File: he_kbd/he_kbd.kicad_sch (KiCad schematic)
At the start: 54 parts, among them J1 AudioJack4, J2 Conn_01x08_Pin

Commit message: updating schematic, realised missing changes from other branch
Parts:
- removed R7, R8, R9: 10k, Resistor_SMD:R_0805_2012Metric_Pad1.20x1.40mm_HandSolder, symbol PCM_SL_Resistors:10k
- added C10, C11, C12, C13, C14, C15, C16, C17, C18, C19, C20, C21, C22, C23, C24, C25, C26, C27, C28, C29, C3, C30, C31, C32, C33, C34, C35, C36, C37, C4, C5, C6, C7, C8, C9: 100n, PCM_Capacitor_SMD_AKL:C_0805_2012Metric_Pad1.18x1.45mm_HandSolder, symbol PCM_Capacitor_AKL:C_0805
- added C38: 500u, PCM_Capacitor_SMD_AKL:C_0805_2012Metric_Pad1.18x1.45mm_HandSolder, symbol PCM_Capacitor_US_AKL:C_0805
- added C39: 100u, PCM_Capacitor_SMD_AKL:C_0805_2012Metric_Pad1.18x1.45mm_HandSolder, symbol PCM_Capacitor_US_AKL:C_0805
- added C40: 50u, PCM_Capacitor_SMD_AKL:C_0805_2012Metric_Pad1.18x1.45mm_HandSolder, symbol PCM_Capacitor_US_AKL:C_0805
- added C41: 20u, PCM_Capacitor_SMD_AKL:C_0805_2012Metric_Pad1.18x1.45mm_HandSolder, symbol PCM_Capacitor_US_AKL:C_0805
- added C42: 10u, PCM_Capacitor_SMD_AKL:C_0805_2012Metric_Pad1.18x1.45mm_HandSolder, symbol PCM_Capacitor_US_AKL:C_0805
- added C51, C_MTP1, C_MTP2, C_MTP3: 100n, PCM_Capacitor_SMD_AKL:C_0805_2012Metric_Pad1.18x1.45mm_HandSolder, symbol PCM_Capacitor_US_AKL:C_0805
- added D1, D10, D11, D12, D13, D14, D15, D16, D17, D18, D19, D2, D20, D21, D22, D23, D24, D25, D26, D27, D28, D29, D3, D30, D31, D32, D33, D34, D35, D4, D5, D6, D7, D8, D9: WS2812B, LED_SMD:LED_WS2812B_PLCC4_5.0x5.0mm_P3.2mm, symbol LED:WS2812B
- added R1, R10, R14, R2, R3: 420, Resistor_SMD:R_0805_2012Metric_Pad1.20x1.40mm_HandSolder, symbol PCM_SL_Resistors:10k
- added SW1, SW10, SW11, SW12, SW13, SW14, SW15, SW16, SW17, SW18, SW19, SW2, SW20, SW21, SW22, SW23, SW24, SW25, SW26, SW27, SW28, SW29, SW3, SW30, SW31, SW32, SW33, SW34, SW35, SW4, SW5, SW6, SW7, SW8, SW9: ~, he_kbd_footprint:SW_Cherry_MX_1.00u_ANALOGUE, symbol he_lib:1u_switch_profile
- C43: value 50u -> 500u
- C44: value 50u -> 100u
- C45, C50: value 50u -> 1u
- C47: value 50u -> 20u
- C48: value 50u -> 100n
- C49: value 50u -> 10u
- R5, R6: value 4.7k -> 10k
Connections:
- net MTP_EN_0 is gone; now on net ANALOGUE_GND: A1.6 (GPIO4), AM0.15 (~{E})
- net MTP_EN_1 is gone; now on net ANALOGUE_GND: A1.7 (GPIO5), AM1.15 (~{E})
- net MTP_EN_2 is gone; now on net ANALOGUE_GND: A1.9 (GPIO6), AM2.15 (~{E})
- net MTP_BIN_0: now also R1.1; no longer A1.1 (GPIO0)
- net MTP_BIN_1: now also R2.1; no longer A1.2 (GPIO1)
- net MTP_BIN_2: now also R3.1; no longer A1.4 (GPIO2)
- net MTP_BIN_3: now also R10.1; no longer A1.5 (GPIO3)
- net NEOPIXEL_DATA: now also R14.1
- net ADC_1: now reaches A1.32 (GPIO27_ADC1)
- net ADC_1: now also AM1.1 (COM)
- net ADC_2: now reaches A1.34 (GPIO28_ADC2)
- net ADC_2: now also AM2.1 (COM)
- net LOCAL_VIN: now reaches A1.40 (VBUS)
- net LOCAL_VIN: now also C45.2, C10.1, C11.1, C12.1, C13.1, C14.1, C15.1, C16.1, C17.1, C18.1, C19.1, C20.1, C21.1, C22.1, C23.1, C24.1, C25.1, C26.1, C27.1, C28.1, C29.1, C3.1, C30.1, C31.1, C32.1, C33.1, C34.1, C35.1, C36.1, C37.1, C38.2, C39.2, C4.1, C40.2, C41.2, C42.2, C5.1, C51.2, C6.1, C7.1, C8.1, C9.1, D1.1 (VDD), D10.1 (VDD), D11.1 (VDD), D12.1 (VDD), D13.1 (VDD), D14.1 (VDD), D15.1 (VDD), D16.1 (VDD), D17.1 (VDD), D18.1 (VDD), D19.1 (VDD), D2.1 (VDD), D20.1 (VDD), D21.1 (VDD), D22.1 (VDD), D23.1 (VDD), D24.1 (VDD), D25.1 (VDD), D26.1 (VDD), D27.1 (VDD), D28.1 (VDD), D29.1 (VDD), D3.1 (VDD), D30.1 (VDD), D31.1 (VDD), D32.1 (VDD), D33.1 (VDD), D34.1 (VDD), D35.1 (VDD), D4.1 (VDD), D5.1 (VDD), D6.1 (VDD), D7.1 (VDD), D8.1 (VDD), D9.1 (VDD)
- net ANALOGUE_VIN renamed 3V3
- net 3V3: now also J1.T, R5.2, R6.1, C_MTP1.2, C_MTP2.2; no longer C45.1
- net AN_SIG renamed ADC_0
- net ADC_0: no longer AM1.1 (COM), AM2.1 (COM)
- net GND renamed ANALOGUE_GND
- net ANALOGUE_GND: now also C45.1, C38.1, C39.1, C40.1, C41.1, C42.1, C51.1, C_MTP1.1, C_MTP2.1, C_MTP3.1; no longer C45.2
- net I2C0_SCL renamed I2C_0_SCL
- net I2C0_SDA renamed I2C_0_SDA
- removed net NEOPIXEL_POWER: A1.39 (VSYS), J1.T, R5.2, R6.1
- new net: D12.2 (DOUT), D13.4 (DIN)
- new net: D11.2 (DOUT), D12.4 (DIN)
- new net: D16.2 (DOUT), D17.4 (DIN)
- new net: D15.2 (DOUT), D16.4 (DIN)
- new net: D8.2 (DOUT), D9.4 (DIN)
- new net: D7.2 (DOUT), D8.4 (DIN)
- new net: A1.1 (GPIO0), R1.2
- new net: A1.5 (GPIO3), R10.2
- new net: D22.2 (DOUT), D23.4 (DIN)
- new net: D21.2 (DOUT), D22.4 (DIN)
- new net: D13.2 (DOUT), D14.4 (DIN)
- new net: D18.2 (DOUT), D19.4 (DIN)
- new net: D17.2 (DOUT), D18.4 (DIN)
- new net: D1.2 (DOUT), D2.4 (DIN)
- new net: D1.4 (DIN), R14.2
- new net: D6.2 (DOUT), D7.4 (DIN)
- new net: D5.2 (DOUT), D6.4 (DIN)
- new net: D4.2 (DOUT), D5.4 (DIN)
- new net: D25.2 (DOUT), D26.4 (DIN)
- new net: D24.2 (DOUT), D25.4 (DIN)
- new net: D27.2 (DOUT), D28.4 (DIN)
- new net: D26.2 (DOUT), D27.4 (DIN)
- new net: D3.2 (DOUT), D4.4 (DIN)
- new net: A1.2 (GPIO1), R2.2
- new net: A1.4 (GPIO2), R3.2
- new net: D14.2 (DOUT), D15.4 (DIN)
- new net: D34.2 (DOUT), D35.4 (DIN)
- new net: D33.2 (DOUT), D34.4 (DIN)
- new net: D19.2 (DOUT), D20.4 (DIN)
- new net: D10.4 (DIN), D9.2 (DOUT)
- new net: D23.2 (DOUT), D24.4 (DIN)
- new net: D32.2 (DOUT), D33.4 (DIN)
- new net: D10.2 (DOUT), D11.4 (DIN)
- new net: D30.2 (DOUT), D31.4 (DIN)
- new net: D29.2 (DOUT), D30.4 (DIN)
- new net: D28.2 (DOUT), D29.4 (DIN)
- new net: D31.2 (DOUT), D32.4 (DIN)
- new net: D20.2 (DOUT), D21.4 (DIN)
- new net: D2.2 (DOUT), D3.4 (DIN)
- new net LOCAL_GND: C10.2, C11.2, C12.2, C13.2, C14.2, C15.2, C16.2, C17.2, C18.2, C19.2, C20.2, C21.2, C22.2, C23.2, C24.2, C25.2, C26.2, C27.2, C28.2, C29.2, C3.2, C30.2, C31.2, C32.2, C33.2, C34.2, C35.2, C36.2, C37.2, C4.2, C5.2, C6.2, C7.2, C8.2, C9.2, D1.3 (VSS), D10.3 (VSS), D11.3 (VSS), D12.3 (VSS), D13.3 (VSS), D14.3 (VSS), D15.3 (VSS), D16.3 (VSS), D17.3 (VSS), D18.3 (VSS), D19.3 (VSS), D2.3 (VSS), D20.3 (VSS), D21.3 (VSS), D22.3 (VSS), D23.3 (VSS), D24.3 (VSS), D25.3 (VSS), D26.3 (VSS), D27.3 (VSS), D28.3 (VSS), D29.3 (VSS), D3.3 (VSS), D30.3 (VSS), D31.3 (VSS), D32.3 (VSS), D33.3 (VSS), D34.3 (VSS), D35.3 (VSS), D4.3 (VSS), D5.3 (VSS), D6.3 (VSS), D7.3 (VSS), D8.3 (VSS), D9.3 (VSS)
- new net VSYS: A1.39 (VSYS)
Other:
- removed sheet Switch profiles
- removed sheet leds
- note added: "Hall effect Sensors - GH39FKSW"
- note added: "Neopixels"
- note added: "Raspberry Pi Pico - rp2040"
- note removed: "Hall effect Sensors / Transistors"
- moved on the sheet: A1, AM0, AM1, AM2, C43, C44, C46, C47, C48, C49, C50, HE_1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

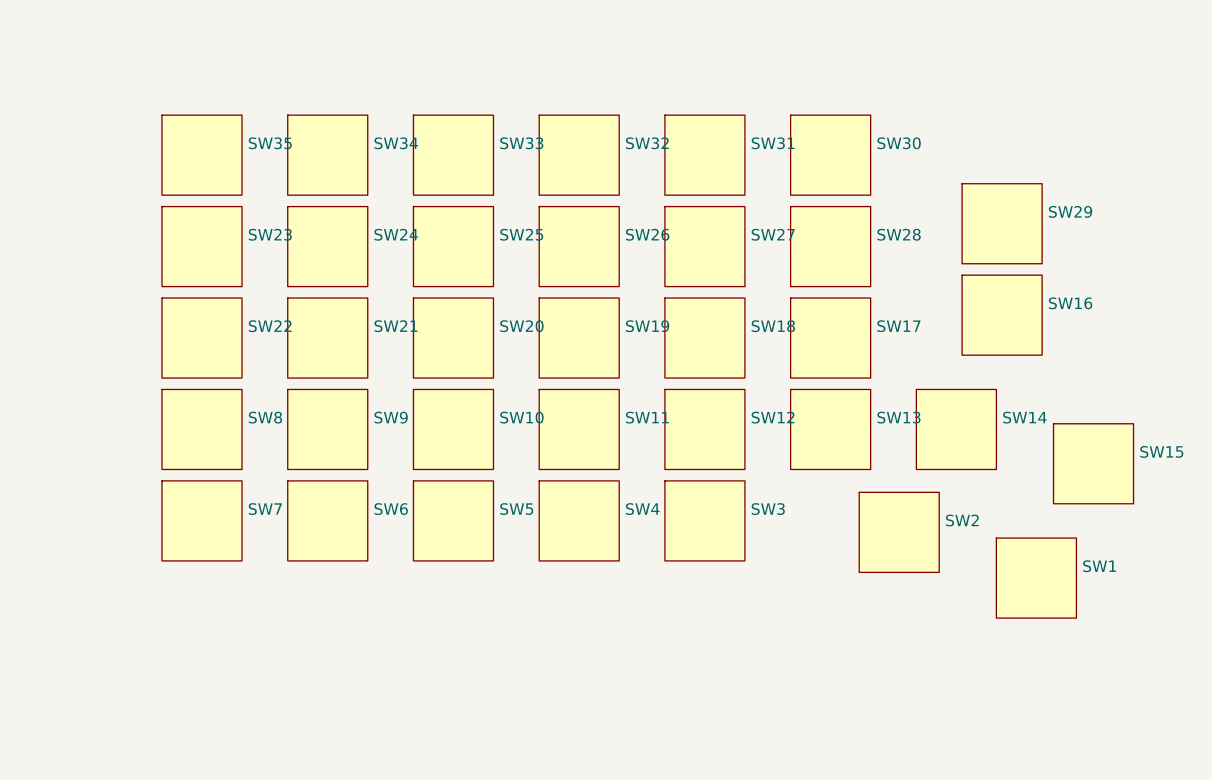
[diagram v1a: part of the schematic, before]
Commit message: tested footprint, updated schematics
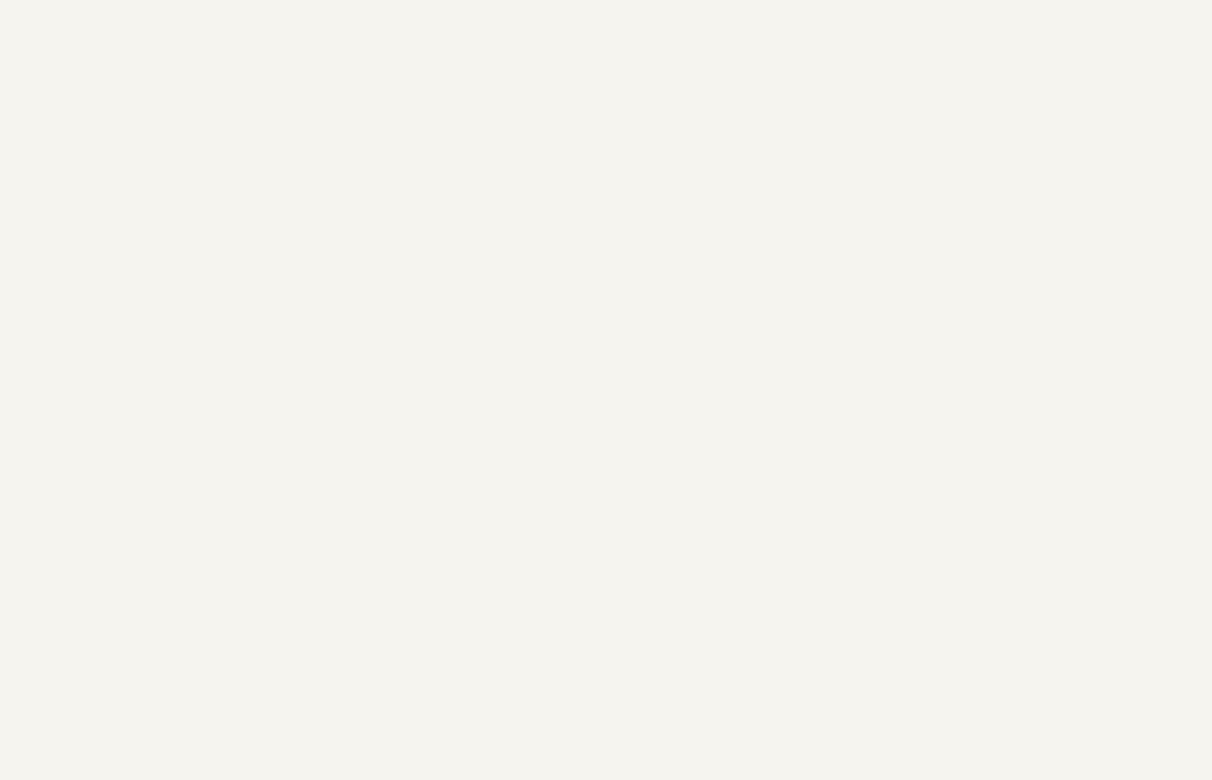
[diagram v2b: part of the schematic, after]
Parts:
- removed SW1, SW10, SW11, SW12, SW13, SW14, SW15, SW16, SW17, SW18, SW19, SW2, SW20, SW21, SW22, SW23, SW24, SW25, SW26, SW27, SW28, SW29, SW3, SW30, SW31, SW32, SW33, SW34, SW35, SW4, SW5, SW6, SW7, SW8, SW9: ~, he_kbd_footprint:SW_Cherry_MX_1.00u_ANALOGUE, symbol he_lib:1u_switch_profile
- HE_1, HE_10, HE_11, HE_12, HE_13, HE_14, HE_15, HE_16, HE_17, HE_18, HE_19, HE_2, HE_20, HE_21, HE_22, HE_23, HE_24, HE_25, HE_26, HE_27, HE_28, HE_29, HE_3, HE_30, HE_31, HE_32, HE_33, HE_34, HE_35, HE_4, HE_5, HE_6, HE_7, HE_8, HE_9: footprint Package_TO_SOT_SMD:SOT-23-3 -> he_kbd_footprint:Analogue_sensor_and_switch_profile
- J1: footprint (none) -> Connector_Audio:Jack_3.5mm_CUI_SJ2-3593D-SMT_Horizontal

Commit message: updated schematic hopefully nets correct now
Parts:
- C42: value 10u -> 100n
- renumbered C_MTP3 to C_MTP0
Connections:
- net LOCAL_GND is gone; now on net ANALOGUE_GND: C10.2, C11.2, C12.2, C13.2, C14.2, C15.2, C16.2, C17.2, C18.2, C19.2, C20.2, C21.2, C22.2, C23.2, C24.2, C25.2, C26.2, C27.2, C28.2, C29.2, C3.2, C30.2, C31.2, C32.2, C33.2, C34.2, C35.2, C36.2, C37.2, C4.2, C5.2, C6.2, C7.2, C8.2, C9.2, D1.3 (VSS), D10.3 (VSS), D11.3 (VSS), D12.3 (VSS), D13.3 (VSS), D14.3 (VSS), D15.3 (VSS), D16.3 (VSS), D17.3 (VSS), D18.3 (VSS), D19.3 (VSS), D2.3 (VSS), D20.3 (VSS), D21.3 (VSS), D22.3 (VSS), D23.3 (VSS), D24.3 (VSS), D25.3 (VSS), D26.3 (VSS), D27.3 (VSS), D28.3 (VSS), D29.3 (VSS), D3.3 (VSS), D30.3 (VSS), D31.3 (VSS), D32.3 (VSS), D33.3 (VSS), D34.3 (VSS), D35.3 (VSS), D4.3 (VSS), D5.3 (VSS), D6.3 (VSS), D7.3 (VSS), D8.3 (VSS), D9.3 (VSS)
- net 3V3: now also C_MTP0.2
- net ANALOGUE_GND: no longer A1.6 (GPIO4), A1.7 (GPIO5), A1.9 (GPIO6)
- net LOCAL_VIN renamed NEOPIXEL_POWER

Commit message: started on both sides flip pcb
updated names

added rhs components to pcb

aligned all left hand side key profiles
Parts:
- added C1, C2, C52, C53, C54, C56, C57, C58, C59, C60, C62, C63, C64, C65, C66, C68, C69, C71, C72, C74, C75, C76, C77, C79, C80, C81, C82, C84, C85, C86, C87, C88, C89, C90, C91: 100n, PCM_Capacitor_SMD_AKL:C_0805_2012Metric_Pad1.18x1.45mm_HandSolder, symbol PCM_Capacitor_AKL:C_0805
- added D36, D37, D38, D39, D40, D41, D42, D43, D44, D45, D46, D47, D48, D49, D50, D51, D52, D53, D54, D55, D56, D57, D58, D59, D60, D61, D62, D63, D64, D65, D66, D67, D68, D69, D70: WS2812B, LED_SMD:LED_WS2812B_PLCC4_5.0x5.0mm_P3.2mm, symbol LED:WS2812B
- added HE_36, HE_37, HE_38, HE_39, HE_40, HE_41, HE_42, HE_43, HE_44, HE_45, HE_46, HE_47, HE_48, HE_49, HE_50, HE_51, HE_52, HE_53, HE_54, HE_55, HE_56, HE_57, HE_58, HE_59, HE_60, HE_61, HE_62, HE_63, HE_64, HE_65, HE_66, HE_67, HE_68, HE_69, HE_70: ~, he_kbd_footprint:Analogue_sensor_and_switch_profile, symbol he_lib:GH39FKSW
- added J3: AudioJack4, Connector_Audio:Jack_3.5mm_CUI_SJ2-3593D-SMT_Horizontal, symbol Connector_Audio:AudioJack4
- added J4: Conn_01x08_Pin, Connector_PinHeader_1.27mm:PinHeader_1x08_P1.27mm_Horizontal, symbol Connector:Conn_01x08_Pin
- added R_C_AN1, R_C_NP1: 500u, PCM_Capacitor_SMD_AKL:C_0805_2012Metric_Pad1.18x1.45mm_HandSolder, symbol PCM_Capacitor_US_AKL:C_0805
- added R_C_AN2, R_C_NP2: 100u, PCM_Capacitor_SMD_AKL:C_0805_2012Metric_Pad1.18x1.45mm_HandSolder, symbol PCM_Capacitor_US_AKL:C_0805
- added R_C_AN3, R_C_NP3: 50u, PCM_Capacitor_SMD_AKL:C_0805_2012Metric_Pad1.18x1.45mm_HandSolder, symbol PCM_Capacitor_US_AKL:C_0805
- added R_C_AN4, R_C_NP4: 20u, PCM_Capacitor_SMD_AKL:C_0805_2012Metric_Pad1.18x1.45mm_HandSolder, symbol PCM_Capacitor_US_AKL:C_0805
- added R_C_AN5: 10u, PCM_Capacitor_SMD_AKL:C_0805_2012Metric_Pad1.18x1.45mm_HandSolder, symbol PCM_Capacitor_US_AKL:C_0805
- added R_C_AN6, R_C_NP6: 1u, PCM_Capacitor_SMD_AKL:C_0805_2012Metric_Pad1.18x1.45mm_HandSolder, symbol PCM_Capacitor_US_AKL:C_0805
- added R_C_AN7, R_C_MTP0, R_C_MTP1, R_C_MTP2, R_C_NP5, R_C_NP7: 100n, PCM_Capacitor_SMD_AKL:C_0805_2012Metric_Pad1.18x1.45mm_HandSolder, symbol PCM_Capacitor_US_AKL:C_0805
- added R_MTP0, R_MTP1, R_MTP2: CD74HC4067M, Package_SO:SSOP-24_5.3x8.2mm_P0.65mm, symbol 74xx:CD74HC4067M
- added R_RPI1: RaspberryPi_Pico, Module:RaspberryPi_Pico_Common_SMD, symbol MCU_Module:RaspberryPi_Pico
- added R_R_BIN0, R_R_BIN1, R_R_BIN2, R_R_BIN3, R_R_NP1: 420, Resistor_SMD:R_0805_2012Metric_Pad1.20x1.40mm_HandSolder, symbol PCM_SL_Resistors:10k
- added R_R_I2C_SDA1, R_R_I2C_SDA2: 10k, Resistor_SMD:R_0805_2012Metric_Pad1.20x1.40mm_HandSolder, symbol PCM_SL_Resistors:4.7k
- renumbered C43 to L_C_AN1, C44 to L_C_AN2, C46 to L_C_AN3, C47 to L_C_AN4, C49 to L_C_AN5, C50 to L_C_AN6, C48 to L_C_AN7, C_MTP0 to L_C_MTP0, C_MTP1 to L_C_MTP1, C_MTP2 to L_C_MTP2, C38 to L_C_NP_0, C39 to L_C_NP_1, C40 to L_C_NP_2, C41 to L_C_NP_3, C42 to L_C_NP_4, C45 to L_C_NP_5, C51 to L_C_NP_6, AM0 to L_MTP0, AM1 to L_MTP1, AM2 to L_MTP2, A1 to L_RPI1, R1 to L_R_BIN0, R2 to L_R_BIN1, R3 to L_R_BIN2, R10 to L_R_BIN3, R6 to L_R_I2C_SCL1, R5 to L_R_I2C_SDA1, R14 to L_R_NP1
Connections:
- net 3V3: now also HE_36.1 (VIN), HE_37.1 (VIN), HE_38.1 (VIN), HE_39.1 (VIN), HE_40.1 (VIN), HE_41.1 (VIN), HE_42.1 (VIN), HE_43.1 (VIN), HE_44.1 (VIN), HE_45.1 (VIN), HE_46.1 (VIN), HE_47.1 (VIN), HE_48.1 (VIN), HE_49.1 (VIN), HE_50.1 (VIN), HE_51.1 (VIN), HE_52.1 (VIN), HE_53.1 (VIN), HE_54.1 (VIN), HE_55.1 (VIN), HE_56.1 (VIN), HE_57.1 (VIN), HE_58.1 (VIN), HE_59.1 (VIN), HE_60.1 (VIN), HE_61.1 (VIN), HE_62.1 (VIN), HE_63.1 (VIN), HE_64.1 (VIN), HE_65.1 (VIN), HE_66.1 (VIN), HE_67.1 (VIN), HE_68.1 (VIN), HE_69.1 (VIN), HE_70.1 (VIN), J3.T, R_C_AN1.1, R_C_AN2.1, R_C_AN3.1, R_C_AN4.1, R_C_AN5.1, R_C_AN6.1, R_C_AN7.1, R_C_MTP0.2, R_C_MTP1.2, R_C_MTP2.2, R_MTP0.24 (VCC), R_MTP1.24 (VCC), R_MTP2.24 (VCC), R_RPI1.36 (3V3), R_R_I2C_SDA1.2, R_R_I2C_SDA2.1
- net ADC_0: now also R_MTP0.1 (COM), R_RPI1.31 (GPIO26_ADC0)
- net ADC_1: now also R_MTP1.1 (COM), R_RPI1.32 (GPIO27_ADC1)
- net ADC_2: now also R_MTP2.1 (COM), R_RPI1.34 (GPIO28_ADC2)
- net ANALOGUE_GND: now also C1.2, C2.2, C52.2, C53.2, C54.2, C56.2, C57.2, C58.2, C59.2, C60.2, C62.2, C63.2, C64.2, C65.2, C66.2, C68.2, C69.2, C71.2, C72.2, C74.2, C75.2, C76.2, C77.2, C79.2, C80.2, C81.2, C82.2, C84.2, C85.2, C86.2, C87.2, C88.2, C89.2, C90.2, C91.2, D36.3 (VSS), D37.3 (VSS), D38.3 (VSS), D39.3 (VSS), D40.3 (VSS), D41.3 (VSS), D42.3 (VSS), D43.3 (VSS), D44.3 (VSS), D45.3 (VSS), D46.3 (VSS), D47.3 (VSS), D48.3 (VSS), D49.3 (VSS), D50.3 (VSS), D51.3 (VSS), D52.3 (VSS), D53.3 (VSS), D54.3 (VSS), D55.3 (VSS), D56.3 (VSS), D57.3 (VSS), D58.3 (VSS), D59.3 (VSS), D60.3 (VSS), D61.3 (VSS), D62.3 (VSS), D63.3 (VSS), D64.3 (VSS), D65.3 (VSS), D66.3 (VSS), D67.3 (VSS), D68.3 (VSS), D69.3 (VSS), D70.3 (VSS), HE_36.3 (GND), HE_37.3 (GND), HE_38.3 (GND), HE_39.3 (GND), HE_40.3 (GND), HE_41.3 (GND), HE_42.3 (GND), HE_43.3 (GND), HE_44.3 (GND), HE_45.3 (GND), HE_46.3 (GND), HE_47.3 (GND), HE_48.3 (GND), HE_49.3 (GND), HE_50.3 (GND), HE_51.3 (GND), HE_52.3 (GND), HE_53.3 (GND), HE_54.3 (GND), HE_55.3 (GND), HE_56.3 (GND), HE_57.3 (GND), HE_58.3 (GND), HE_59.3 (GND), HE_60.3 (GND), HE_61.3 (GND), HE_62.3 (GND), HE_63.3 (GND), HE_64.3 (GND), HE_65.3 (GND), HE_66.3 (GND), HE_67.3 (GND), HE_68.3 (GND), HE_69.3 (GND), HE_70.3 (GND), J3.S, R_C_AN1.2, R_C_AN2.2, R_C_AN3.2, R_C_AN4.2, R_C_AN5.2, R_C_AN6.2, R_C_AN7.2, R_C_MTP0.1, R_C_MTP1.1, R_C_MTP2.1, R_C_NP1.1, R_C_NP2.1, R_C_NP3.1, R_C_NP4.1, R_C_NP5.1, R_C_NP6.1, R_C_NP7.1, R_MTP0.12 (GND), R_MTP0.15 (~{E}), R_MTP1.12 (GND), R_MTP1.15 (~{E}), R_MTP2.12 (GND), R_MTP2.15 (~{E}), R_RPI1.13 (GND), R_RPI1.18 (GND), R_RPI1.23 (GND), R_RPI1.28 (GND), R_RPI1.3 (GND), R_RPI1.38 (GND), R_RPI1.8 (GND)
- net I2C_0_SCL: now also J3.R1, R_RPI1.27 (GPIO21), R_R_I2C_SDA2.2
- net I2C_0_SDA: now also J3.R2, R_RPI1.26 (GPIO20), R_R_I2C_SDA1.1
- net MTP_BIN_0: now also R_MTP0.10 (S0), R_MTP1.10 (S0), R_MTP2.10 (S0), R_R_BIN0.1
- net MTP_BIN_1: now also R_MTP0.11 (S1), R_MTP1.11 (S1), R_MTP2.11 (S1), R_R_BIN1.1
- net MTP_BIN_2: now also R_MTP0.14 (S2), R_MTP1.14 (S2), R_MTP2.14 (S2), R_R_BIN2.1
- net MTP_BIN_3: now also R_MTP0.13 (S3), R_MTP1.13 (S3), R_MTP2.13 (S3), R_R_BIN3.1
- net NEOPIXEL_DATA: now also R_RPI1.21 (GPIO16), R_R_NP1.1
- net NEOPIXEL_POWER: now also C1.1, C2.1, C52.1, C53.1, C54.1, C56.1, C57.1, C58.1, C59.1, C60.1, C62.1, C63.1, C64.1, C65.1, C66.1, C68.1, C69.1, C71.1, C72.1, C74.1, C75.1, C76.1, C77.1, C79.1, C80.1, C81.1, C82.1, C84.1, C85.1, C86.1, C87.1, C88.1, C89.1, C90.1, C91.1, D36.1 (VDD), D37.1 (VDD), D38.1 (VDD), D39.1 (VDD), D40.1 (VDD), D41.1 (VDD), D42.1 (VDD), D43.1 (VDD), D44.1 (VDD), D45.1 (VDD), D46.1 (VDD), D47.1 (VDD), D48.1 (VDD), D49.1 (VDD), D50.1 (VDD), D51.1 (VDD), D52.1 (VDD), D53.1 (VDD), D54.1 (VDD), D55.1 (VDD), D56.1 (VDD), D57.1 (VDD), D58.1 (VDD), D59.1 (VDD), D60.1 (VDD), D61.1 (VDD), D62.1 (VDD), D63.1 (VDD), D64.1 (VDD), D65.1 (VDD), D66.1 (VDD), D67.1 (VDD), D68.1 (VDD), D69.1 (VDD), D70.1 (VDD), R_C_NP1.2, R_C_NP2.2, R_C_NP3.2, R_C_NP4.2, R_C_NP5.2, R_C_NP6.2, R_C_NP7.2, R_RPI1.40 (VBUS)
- net VSYS: now also R_RPI1.39 (VSYS)
- net hesig1: now also HE_44.2 (OUT), R_MTP0.9 (I0)
- net hesig10: now also HE_42.2 (OUT), R_MTP0.22 (I9)
- net hesig11: now also HE_41.2 (OUT), R_MTP0.21 (I10)
- net hesig12: now also HE_40.2 (OUT), R_MTP0.20 (I11)
- net hesig13: now also HE_39.2 (OUT), R_MTP0.19 (I12)
- net hesig14: now also HE_38.2 (OUT), R_MTP0.18 (I13)
- net hesig15: now also HE_37.2 (OUT), R_MTP0.17 (I14)
- net hesig16: now also HE_36.2 (OUT), R_MTP0.16 (I15)
- net hesig17: now also HE_60.2 (OUT), R_MTP1.9 (I0)
- net hesig18: now also HE_61.2 (OUT), R_MTP1.8 (I1)
- net hesig19: now also HE_62.2 (OUT), R_MTP1.7 (I2)
- net hesig2: now also HE_45.2 (OUT), R_MTP0.8 (I1)
- net hesig20: now also HE_63.2 (OUT), R_MTP1.6 (I3)
- net hesig21: now also HE_64.2 (OUT), R_MTP1.5 (I4)
- net hesig22: now also HE_65.2 (OUT), R_MTP1.4 (I5)
- net hesig23: now also HE_66.2 (OUT), R_MTP1.3 (I6)
- net hesig24: now also HE_67.2 (OUT), R_MTP1.2 (I7)
- net hesig25: now also HE_59.2 (OUT), R_MTP1.23 (I8)
- net hesig26: now also HE_58.2 (OUT), R_MTP1.22 (I9)
- net hesig27: now also HE_57.2 (OUT), R_MTP1.21 (I10)
- net hesig28: now also HE_56.2 (OUT), R_MTP1.20 (I11)
- net hesig29: now also HE_55.2 (OUT), R_MTP1.19 (I12)
- net hesig3: now also HE_46.2 (OUT), R_MTP0.7 (I2)
- net hesig30: now also HE_54.2 (OUT), R_MTP1.18 (I13)
- net hesig31: now also HE_53.2 (OUT), R_MTP1.17 (I14)
- net hesig32: now also HE_52.2 (OUT), R_MTP1.16 (I15)
- net hesig33: now also HE_68.2 (OUT), R_MTP2.9 (I0)
- net hesig34: now also HE_69.2 (OUT), R_MTP2.8 (I1)
- net hesig35: now also HE_70.2 (OUT), R_MTP2.7 (I2)
- net hesig4: now also HE_47.2 (OUT), R_MTP0.6 (I3)
- net hesig5: now also HE_48.2 (OUT), R_MTP0.5 (I4)
- net hesig6: now also HE_49.2 (OUT), R_MTP0.4 (I5)
- net hesig7: now also HE_50.2 (OUT), R_MTP0.3 (I6)
- net hesig8: now also HE_51.2 (OUT), R_MTP0.2 (I7)
- net hesig9: now also HE_43.2 (OUT), R_MTP0.23 (I8)
- new net: R_RPI1.5 (GPIO3), R_R_BIN3.2
- new net: D56.2 (DOUT), D60.4 (DIN)
- new net: D52.2 (DOUT), D56.4 (DIN)
- new net: D60.2 (DOUT), D64.4 (DIN)
- new net: R_RPI1.1 (GPIO0), R_R_BIN0.2
- new net: R_RPI1.2 (GPIO1), R_R_BIN1.2
- new net: R_RPI1.4 (GPIO2), R_R_BIN2.2
- new net: D58.4 (DIN), D62.2 (DOUT)
- new net: D62.4 (DIN), D66.2 (DOUT)
- new net: D42.2 (DOUT), D47.4 (DIN)
- new net: D37.2 (DOUT), D42.4 (DIN)
- new net: D49.4 (DIN), D54.2 (DOUT)
- new net: D54.4 (DIN), D58.2 (DOUT)
- new net: D41.4 (DIN), D46.2 (DOUT)
- new net: D46.4 (DIN), D51.2 (DOUT)
- new net: D37.4 (DIN), R_R_NP1.2
- new net: D61.2 (DOUT), D65.4 (DIN)
- new net: D57.2 (DOUT), D61.4 (DIN)
- new net: D48.2 (DOUT), D53.4 (DIN)
- new net: D43.2 (DOUT), D48.4 (DIN)
- new net: D51.4 (DIN), D55.2 (DOUT)
- new net: D55.4 (DIN), D59.2 (DOUT)
- new net: D47.2 (DOUT), D52.4 (DIN)
- new net: D45.2 (DOUT), D50.4 (DIN)
- new net: D40.2 (DOUT), D45.4 (DIN)
- new net: D44.4 (DIN), D49.2 (DOUT)
- new net: J4.4 (Pin_4), R_MTP2.2 (I7)
- new net: J4.1 (Pin_1), R_MTP2.21 (I10)
- new net: J4.2 (Pin_2), R_MTP2.22 (I9)
- new net: J4.3 (Pin_3), R_MTP2.23 (I8)
- new net: J4.5 (Pin_5), R_MTP2.3 (I6)
- new net: J4.6 (Pin_6), R_MTP2.4 (I5)
- new net: J4.7 (Pin_7), R_MTP2.5 (I4)
- new net: J4.8 (Pin_8), R_MTP2.6 (I3)
- new net: D39.2 (DOUT), D40.4 (DIN)
- new net: D39.4 (DIN), D44.2 (DOUT)
- new net: D66.4 (DIN), D70.2 (DOUT)
- new net: D63.4 (DIN), D67.2 (DOUT)
- new net: D67.4 (DIN), D68.2 (DOUT)
- new net: D69.2 (DOUT), D70.4 (DIN)
- new net: D65.2 (DOUT), D69.4 (DIN)
- new net: D36.4 (DIN), D41.2 (DOUT)
- new net: D59.4 (DIN), D63.2 (DOUT)
- new net: D53.2 (DOUT), D57.4 (DIN)
- new net: D64.2 (DOUT), D68.4 (DIN)
- new net: D36.2 (DOUT), D38.4 (DIN)
- new net: D38.2 (DOUT), D43.4 (DIN)
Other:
- note added: "Left"
- note added: "Right"
- moved on the sheet: C10, C11, C12, C13, C14, C15, C16, C17, C18, C19, C20, C21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
